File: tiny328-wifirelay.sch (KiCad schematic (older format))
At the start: 8 parts, among them P1 RX868SH-DV, U1 TINY328, U2 ESP-01v090, U3 LD1117S33TR

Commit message: updated for PCB run #1
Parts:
- added D1, D2, D3, D4: LED, LEDs:LED-0805, symbol LED
- added R2, R3, R4, R5: 68, Resistors_SMD:R_0603_HandSoldering, symbol R
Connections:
- wire segments 27 -> 45
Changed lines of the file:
@@
 Connection ~ 5450 3050
 Wire Wire Line
-	5700 3400 5000 3400
-Wire Wire Line
-	5050 3400 4550 3400
+	4550 3400 5700 3400
 Connection ~ 5000 3400
 Wire Wire Line
@@
 Connection ~ 5400 3400
 Connection ~ 5450 3400
+$Comp
+L R R5
+U 1 1 55E88AAB
+P 5100 1850
+F 0 "R5" V 5180 1850 50  0000 C CNN
+F 1 "68" V 5100 1850 50  0000 C CNN
+F 2 "Resistors_SMD:R_0603_HandSoldering" V 5030 1850 30  0001 C CNN
+F 3 "" H 5100 1850 30  0000 C CNN
+	1    5100 1850
+	0    1    1    0
+$EndComp
+$Comp
+L R R4
+U 1 1 55E88AED
+P 5100 1700
+F 0 "R4" V 5180 1700 50  0000 C CNN
+F 1 "68" V 5100 1700 50  0000 C CNN
+F 2 "Resistors_SMD:R_0603_HandSoldering" V 5030 1700 30  0001 C CNN
+F 3 "" H 5100 1700 30  0000 C CNN
+	1    5100 1700
+	0    1    1    0
+$EndComp
+$Comp
+L R R3
+U 1 1 55E88B16
+P 5100 1400
+F 0 "R3" V 5180 1400 50  0000 C CNN
+F 1 "68" V 5100 1400 50  0000 C CNN
+F 2 "Resistors_SMD:R_0603_HandSoldering" V 5030 1400 30  0001 C CNN
+F 3 "" H 5100 1400 30  0000 C CNN
+	1    5100 1400
+	0    1    1    0
+$EndComp
+$Comp
+L R R2
+U 1 1 55E88B3C
+P 5100 1250
+F 0 "R2" V 5180 1250 50  0000 C CNN
+F 1 "68" V 5100 1250 50  0000 C CNN
+F 2 "Resistors_SMD:R_0603_HandSoldering" V 5030 1250 30  0000 C CNN
+F 3 "" H 5100 1250 30  0000 C CNN
+	1    5100 1250
+	0    1    1    0
+$EndComp
+$Comp
+L LED D1
+U 1 1 55E88D78
+P 5550 1250
+F 0 "D1" H 5550 1350 50  0000 C CNN
+F 1 "LED" H 5550 1150 50  0000 C CNN
+F 2 "LEDs:LED-0805" H 5550 1250 60  0001 C CNN
+F 3 "" H 5550 1250 60  0000 C CNN
+	1    5550 1250
+	1    0    0    -1
+$EndComp
+$Comp
+L LED D2
+U 1 1 55E88DA6
+P 5550 1400
+F 0 "D2" H 5550 1500 50  0000 C CNN
+F 1 "LED" H 5550 1300 50  0000 C CNN
+F 2 "LEDs:LED-0805" H 5550 1400 60  0001 C CNN
+F 3 "" H 5550 1400 60  0000 C CNN
+	1    5550 1400
+	1    0    0    -1
+$EndComp
+$Comp
+L LED D3
+U 1 1 55E88DCB
+P 5550 1700
+F 0 "D3" H 5550 1800 50  0000 C CNN
+F 1 "LED" H 5550 1600 50  0000 C CNN
+F 2 "LEDs:LED-0805" H 5550 1700 60  0001 C CNN
+F 3 "" H 5550 1700 60  0000 C CNN
+	1    5550 1700
+	1    0    0    -1
+$EndComp
+$Comp
+L LED D4
+U 1 1 55E88DF3
+P 5550 1850
+F 0 "D4" H 5550 1950 50  0000 C CNN
+F 1 "LED" H 5550 1750 50  0000 C CNN
+F 2 "LEDs:LED-0805" H 5550 1850 60  0001 C CNN
+F 3 "" H 5550 1850 60  0000 C CNN
+	1    5550 1850
+	1    0    0    -1
+$EndComp
+Wire Wire Line
+	4450 1800 4850 1800
+Wire Wire Line
+	4850 1800 4850 1850
+Wire Wire Line
+	4850 1850 4950 1850
+Wire Wire Line
+	4950 1700 4450 1700
+Wire Wire Line
+	5250 1700 5350 1700
+Wire Wire Line
+	5250 1850 5350 1850
+Wire Wire Line
+	5250 1400 5350 1400
+Wire Wire Line
+	4450 1500 4850 1500
+Wire Wire Line
+	4850 1500 4850 1400
+Wire Wire Line
+	4850 1400 4950 1400
+Wire Wire Line
+	4950 1250 4800 1250
+Wire Wire Line
+	4800 1250 4800 1400
+Wire Wire Line
+	4800 1400 4450 1400
+Wire Wire Line
+	5250 1250 5350 1250
+$Comp
+L GND #PWR011
+U 1 1 55E891D2
+P 5850 1950
+F 0 "#PWR011" H 5850 1700 50  0001 C CNN
+F 1 "GND" H 5850 1800 50  0000 C CNN
+F 2 "" H 5850 1950 60  0000 C CNN
+F 3 "" H 5850 1950 60  0000 C CNN
+	1    5850 1950
+	1    0    0    -1
+$EndComp
+Wire Wire Line
+	5750 1850 5850 1850
+Wire Wire Line
+	5850 1250 5850 1950
+Wire Wire Line
+	5750 1700 5850 1700
+Connection ~ 5850 1850
+Wire Wire Line
+	5750 1400 5850 1400
+Connection ~ 5850 1700
+Wire Wire Line
+	5750 1250 5850 1250
+Connection ~ 5850 1400
 $EndSCHEMATC

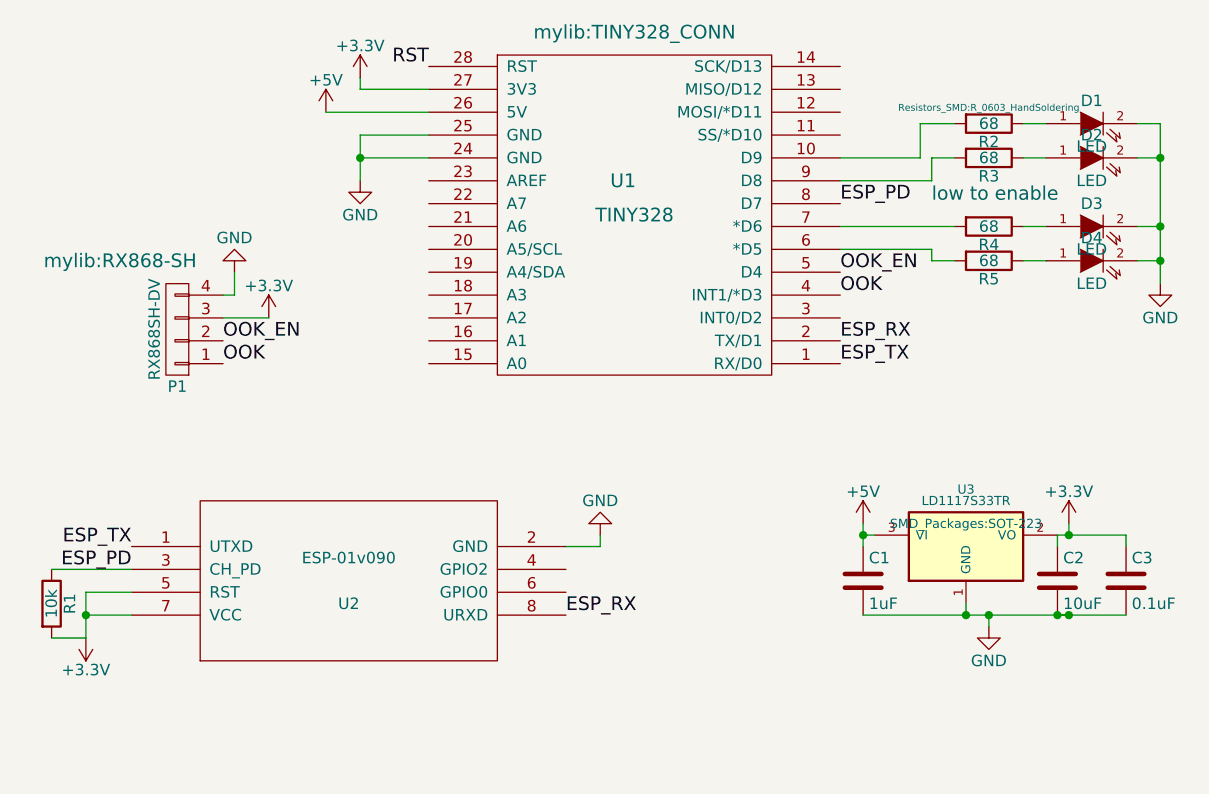
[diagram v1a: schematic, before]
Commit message: Fix ESP initialization
We do this by pulling down CH_PD, such that the ESP doesn't start booting
until the AtMega tells it to.
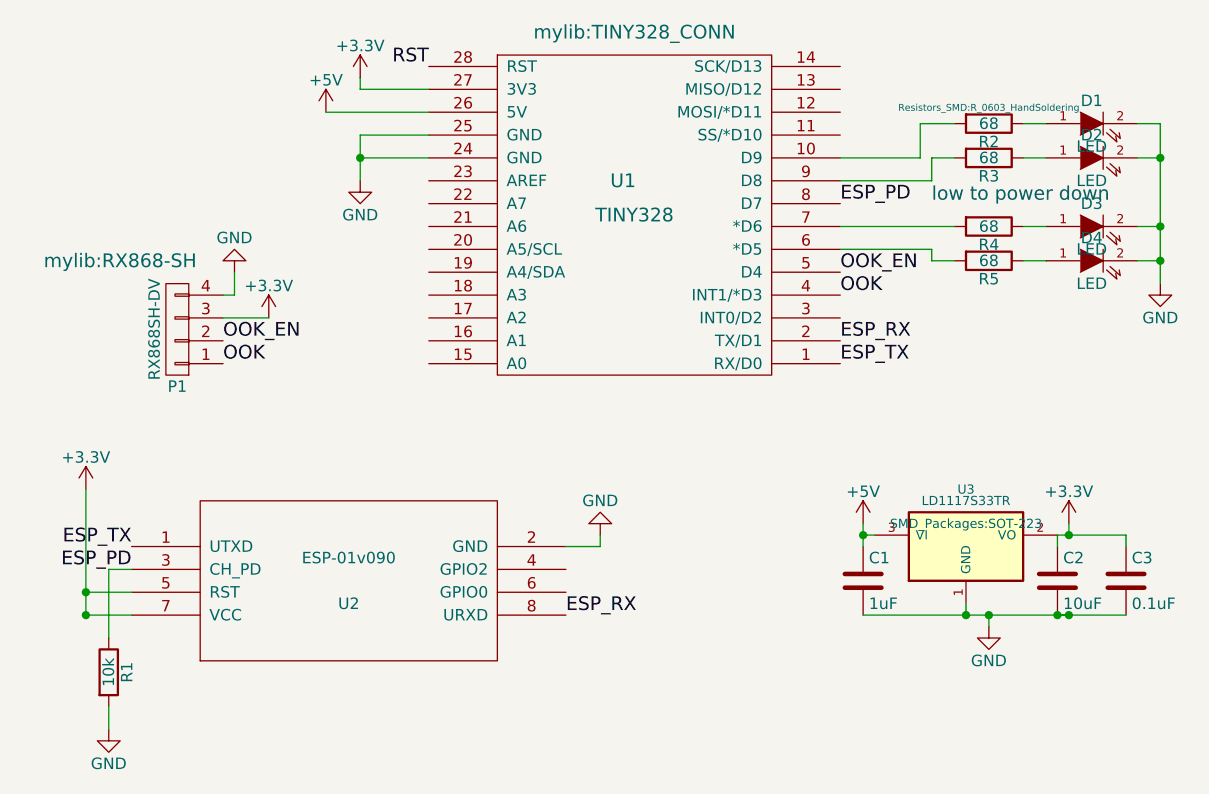
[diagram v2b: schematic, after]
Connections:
- net +3V3: no longer R1.2
- net GND: now also R1.2
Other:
- note added: "low to power down"
- note removed: "low to enable"
- moved on the sheet: R1
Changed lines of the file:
@@
 L +3.3V #PWR04
 U 1 1 55B77763
-P 1150 3500
-F 0 "#PWR04" H 1150 3350 50  0001 C CNN
-F 1 "+3.3V" H 1150 3640 50  0000 C CNN
-F 2 "" H 1150 3500 60  0000 C CNN
-F 3 "" H 1150 3500 60  0000 C CNN
-	1    1150 3500
-	-1   0    0    1
+P 1150 2850
+F 0 "#PWR04" H 1150 2700 50  0001 C CNN
+F 1 "+3.3V" H 1150 2990 50  0000 C CNN
+F 2 "" H 1150 2850 60  0000 C CNN
+F 3 "" H 1150 2850 60  0000 C CNN
+	1    1150 2850
+	1    0    0    -1
 $EndComp
 $Comp
@@
 L R R1
 U 1 1 55B77A99
-P 1000 3350
-F 0 "R1" V 1080 3350 50  0000 C CNN
-F 1 "10k" V 1000 3350 50  0000 C CNN
-F 2 "Resistors_SMD:R_0603_HandSoldering" V 930 3350 30  0001 C CNN
-F 3 "" H 1000 3350 30  0000 C CNN
-	1    1000 3350
-	1    0    0    -1
-$EndComp
-Wire Wire Line
-	1150 3300 1150 3500
+P 1250 3650
+F 0 "R1" V 1330 3650 50  0000 C CNN
+F 1 "10k" V 1250 3650 50  0000 C CNN
+F 2 "Resistors_SMD:R_0603_HandSoldering" V 1180 3650 30  0001 C CNN
+F 3 "" H 1250 3650 30  0000 C CNN
+	1    1250 3650
+	1    0    0    -1
+$EndComp
+Wire Wire Line
+	1150 2850 1150 3400
 Wire Wire Line
 	1150 3400 1350 3400
-Wire Wire Line
-	1350 3200 1000 3200
-Wire Wire Line
-	1150 3500 1000 3500
 Text Label 2650 1000 2    60   ~ 0
 RST
@@
 ESP_PD
 Text Notes 4850 1600 0    60   ~ 0
-low to enable
+low to power down
 $Comp
 L ESP-01v090 U2
@@
 $EndComp
 Wire Wire Line
-	5750 1850 5850 1850
+	5850 1850 5750 1850
 Wire Wire Line
 	5850 1250 5850 1950
@@
 	5750 1250 5850 1250
 Connection ~ 5850 1400
+$Comp
+L GND #PWR?
+U 1 1 563127D7
+P 1250 3900
+F 0 "#PWR?" H 1250 3650 50  0001 C CNN
+F 1 "GND" H 1250 3750 50  0000 C CNN
+F 2 "" H 1250 3900 60  0000 C CNN
+F 3 "" H 1250 3900 60  0000 C CNN
+	1    1250 3900
+	1    0    0    -1
+$EndComp
+Connection ~ 1150 3300
+Wire Wire Line
+	1350 3200 1250 3200
+Wire Wire Line
+	1250 3200 1250 3500
+Wire Wire Line
+	1250 3900 1250 3800
 $EndSCHEMATC
